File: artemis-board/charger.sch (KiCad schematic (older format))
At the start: 25 parts, among them J10 External NTC, J2 Thermistor, Q2 2N7002, SW2 SKRKAEE020, U3 LC709203FQH-01TWG, U4 TP4056, U8 XC6206P332MR

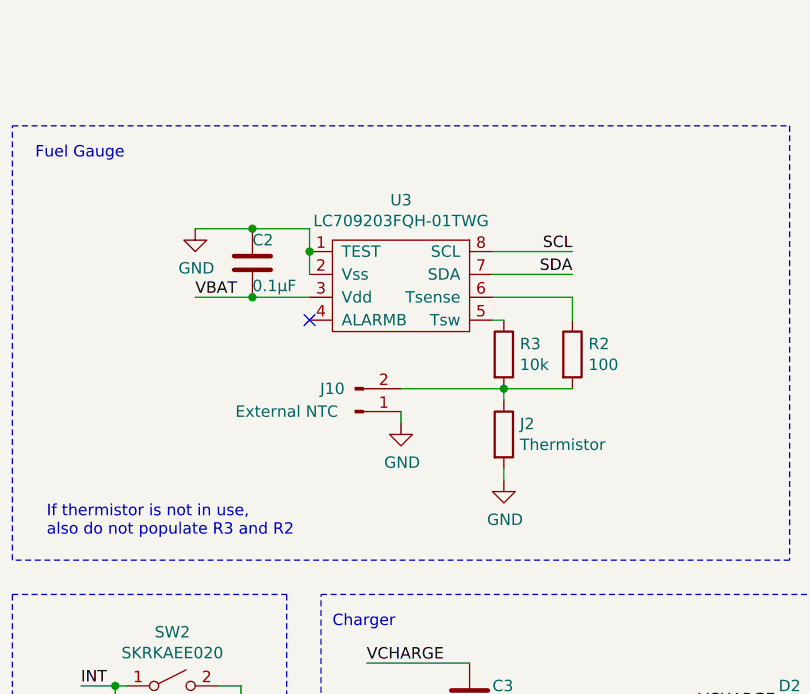
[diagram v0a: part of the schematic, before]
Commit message: removed lc709203 and added MAX17048
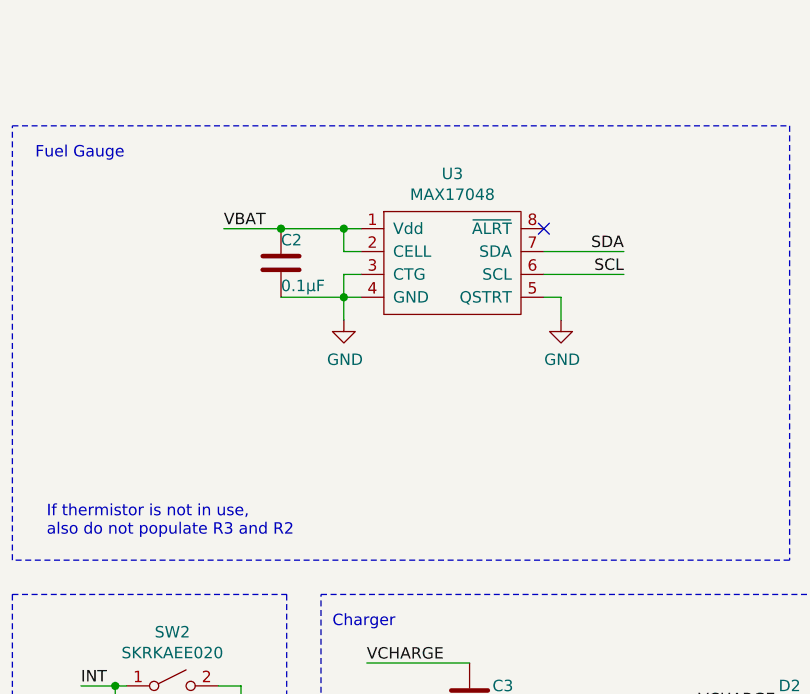
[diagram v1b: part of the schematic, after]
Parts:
- removed J10: External NTC, Connector_PinHeader_2.54mm:PinHeader_1x02_P2.54mm_Vertical, symbol Connector:Conn_01x02_Male
- removed J2: Thermistor, Resistor_SMD:R_0603_1608Metric_Pad1.05x0.95mm_HandSolder, symbol Device:R
- removed R2: 100, Resistor_SMD:R_0603_1608Metric_Pad1.05x0.95mm_HandSolder, symbol Device:R
- removed R3: 10k, Resistor_SMD:R_0603_1608Metric_Pad1.05x0.95mm_HandSolder, symbol Device:R
- removed U3: LC709203FQH-01TWG, Package_DFN_QFN:WDFN-8-1EP_4x3mm_P0.65mm_EP2.4x1.8mm, symbol LC709203FQH:LC709203FQH
- added U3: MAX17048, Package_DFN_QFN:TDFN-8-1EP_2x2mm_P0.5mm_EP0.8x1.2mm, symbol MAX17048:MAX17048
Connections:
- net GND: now also C2.2, U3.3 (CTG), U3.4 (GND), U3.5 (QSTRT); no longer C2.1
- net SCL: now also U3.6 (SCL)
- net SDA: now also U3.7 (SDA)
- net VBAT: now also C2.1, U3.1 (Vdd), U3.2 (CELL); no longer C2.2
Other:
- moved on the sheet: C2
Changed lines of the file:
@@
 	6350 5300 6350 5050
 Wire Wire Line
-	3300 2800 3550 2800
-Text Label 3300 2800 0    50   ~ 0
+	3425 2500 3675 2500
+Text Label 3425 2500 0    50   ~ 0
 VBAT
-Text Label 4950 2600 2    50   ~ 0
+Text Label 5175 2700 2    50   ~ 0
 SCL
-Text Label 4950 2700 2    50   ~ 0
+Text Label 5175 2600 2    50   ~ 0
 SDA
 Wire Wire Line
-	4950 2600 4600 2600
-Wire Wire Line
-	4950 2700 4600 2700
+	5175 2700 4825 2700
+Wire Wire Line
+	5175 2600 4825 2600
 Wire Notes Line
 	2500 2050 5900 2050
-NoConn ~ 3800 2900
-Connection ~ 3550 2800
-$Comp
-L LC709203FQH:LC709203FQH U3
-U 1 1 5F7E175C
-P 4200 2750
-F 0 "U3" H 4200 3125 50  0000 C CNN
-F 1 "LC709203FQH-01TWG" H 4200 3034 50  0000 C CNN
-F 2 "Package_DFN_QFN:WDFN-8-1EP_4x3mm_P0.65mm_EP2.4x1.8mm" H 4250 2500 50  0001 C CNN
-F 3 "https://www.onsemi.com/pub/Collateral/LC709203F-D.PDF" H 4200 2800 50  0001 C CNN
-F 4 "C152311" H 4200 2750 50  0001 C CNN "LCSC"
-	1    4200 2750
-	1    0    0    -1
-$EndComp
-$Comp
-L Device:R R2
-U 1 1 5F7E20B2
-P 4950 3050
-F 0 "R2" H 5020 3096 50  0000 L CNN
-F 1 "100" H 5020 3005 50  0000 L CNN
-F 2 "Resistor_SMD:R_0603_1608Metric_Pad1.05x0.95mm_HandSolder" V 4880 3050 50  0001 C CNN
-F 3 "~" H 4950 3050 50  0001 C CNN
-F 4 "C22775" H 4950 3050 50  0001 C CNN "LCSC"
-	1    4950 3050
-	1    0    0    -1
-$EndComp
-$Comp
-L Device:R R3
-U 1 1 5F7E249E
-P 4650 3050
-F 0 "R3" H 4720 3096 50  0000 L CNN
-F 1 "10k" H 4720 3005 50  0000 L CNN
-F 2 "Resistor_SMD:R_0603_1608Metric_Pad1.05x0.95mm_HandSolder" V 4580 3050 50  0001 C CNN
-F 3 "~" H 4650 3050 50  0001 C CNN
-F 4 "C25804" H 4650 3050 50  0001 C CNN "LCSC"
-	1    4650 3050
-	1    0    0    -1
-$EndComp
 $Comp
 L Device:C C2
 U 1 1 5F7E2A6A
-P 3550 2650
-F 0 "C2" H 3550 2750 50  0000 L CNN
-F 1 "0.1µF" H 3550 2550 50  0000 L CNN
-F 2 "Capacitor_SMD:C_0603_1608Metric_Pad1.05x0.95mm_HandSolder" H 3588 2500 50  0001 C CNN
-F 3 "~" H 3550 2650 50  0001 C CNN
-F 4 "C14858" H 3550 2650 50  0001 C CNN "LCSC"
-	1    3550 2650
-	1    0    0    -1
-$EndComp
-Wire Wire Line
-	4600 2900 4650 2900
-Wire Wire Line
-	4600 2800 4950 2800
-Wire Wire Line
-	4950 2800 4950 2900
-Wire Wire Line
-	4650 3200 4950 3200
-Wire Wire Line
-	3800 2800 3550 2800
-Wire Wire Line
-	3800 2700 3800 2600
-Wire Wire Line
-	3550 2500 3800 2500
-Wire Wire Line
-	3800 2500 3800 2600
-Connection ~ 3800 2600
+P 3675 2650
+F 0 "C2" H 3675 2750 50  0000 L CNN
+F 1 "0.1µF" H 3675 2550 50  0000 L CNN
+F 2 "Capacitor_SMD:C_0603_1608Metric_Pad1.05x0.95mm_HandSolder" H 3713 2500 50  0001 C CNN
+F 3 "~" H 3675 2650 50  0001 C CNN
+F 4 "C14858" H 3675 2650 50  0001 C CNN "LCSC"
+	1    3675 2650
+	1    0    0    -1
+$EndComp
 $Comp
 L power:GND #PWR0105
 U 1 1 5F7E81F4
-P 3300 2500
-F 0 "#PWR0105" H 3300 2250 50  0001 C CNN
-F 1 "GND" H 3305 2327 50  0000 C CNN
-F 2 "" H 3300 2500 50  0001 C CNN
-F 3 "" H 3300 2500 50  0001 C CNN
-	1    3300 2500
-	1    0    0    -1
-$EndComp
-Wire Wire Line
-	3300 2500 3550 2500
-Connection ~ 3550 2500
-$Comp
-L power:GND #PWR0104
-U 1 1 5F7EE01C
-P 4650 3600
-F 0 "#PWR0104" H 4650 3350 50  0001 C CNN
-F 1 "GND" H 4655 3427 50  0000 C CNN
-F 2 "" H 4650 3600 50  0001 C CNN
-F 3 "" H 4650 3600 50  0001 C CNN
-	1    4650 3600
+P 4900 2900
+F 0 "#PWR0105" H 4900 2650 50  0001 C CNN
+F 1 "GND" H 4905 2727 50  0000 C CNN
+F 2 "" H 4900 2900 50  0001 C CNN
+F 3 "" H 4900 2900 50  0001 C CNN
+	1    4900 2900
 	1    0    0    -1
 $EndComp
@@
 	0    1    1    0
 $EndComp
-$Comp
-L Device:R J2
-U 1 1 600A8086
-P 4650 3400
-F 0 "J2" H 4720 3446 50  0000 L CNN
-F 1 "Thermistor" H 4720 3355 50  0000 L CNN
-F 2 "Resistor_SMD:R_0603_1608Metric_Pad1.05x0.95mm_HandSolder" V 4580 3400 50  0001 C CNN
-F 3 "https://datasheet.lcsc.com/szlcsc/TDK-NTCG163JF103FT1_C76589.pdf" H 4650 3400 50  0001 C CNN
-F 4 "C76589" H 4650 3400 50  0001 C CNN "LCSC"
-	1    4650 3400
-	1    0    0    -1
-$EndComp
-Wire Wire Line
-	4650 3550 4650 3600
-Wire Wire Line
-	4650 3250 4650 3200
-Connection ~ 4650 3200
 Text Notes 6100 3900 0    50   ~ 0
 This cirquit automatically pulls down the INT line when first powerd on
@@
 If thermistor is not in use,\nalso do not populate R3 and R2
 $Comp
-L Connector:Conn_01x02_Male J?
-U 1 1 60103514
-P 4000 3300
-AR Path="/5F639CFE/60103514" Ref="J?"  Part="1"
-AR Path="/5F639F48/60103514" Ref="J10"  Part="1"
-F 0 "J10" H 3900 3200 50  0000 C CNN
-F 1 "External NTC" H 3700 3300 50  0000 C CNN
-F 2 "Connector_PinHeader_2.54mm:PinHeader_1x02_P2.54mm_Vertical" H 4000 3300 50  0001 C CNN
-F 3 "" H 4000 3300 50  0001 C CNN
-F 4 "" H 4000 3300 50  0001 C CNN "LCSC"
-F 5 "DNP" H 4000 3300 50  0001 C CNN "DNP"
-	1    4000 3300
-	1    0    0    1
-$EndComp
-Wire Wire Line
-	4650 3200 4200 3200
-$Comp
 L power:GND #PWR0131
 U 1 1 60107260
-P 4200 3350
-F 0 "#PWR0131" H 4200 3100 50  0001 C CNN
-F 1 "GND" H 4205 3177 50  0000 C CNN
-F 2 "" H 4200 3350 50  0001 C CNN
-F 3 "" H 4200 3350 50  0001 C CNN
-	1    4200 3350
-	1    0    0    -1
-$EndComp
-Wire Wire Line
-	4200 3300 4200 3350
+P 3950 2900
+F 0 "#PWR0131" H 3950 2650 50  0001 C CNN
+F 1 "GND" H 3955 2727 50  0000 C CNN
+F 2 "" H 3950 2900 50  0001 C CNN
+F 3 "" H 3950 2900 50  0001 C CNN
+	1    3950 2900
+	1    0    0    -1
+$EndComp
 $Comp
 L Switch:SW_SPST SW?
@@
 Wire Notes Line
 	2000 6050 4350 6050
+$Comp
+L MAX17048:MAX17048 U?
+U 1 1 626AEF97
+P 4425 2325
+AR Path="/626AEF97" Ref="U?"  Part="1"
+AR Path="/5F639F48/626AEF97" Ref="U3"  Part="1"
+F 0 "U3" H 4425 2390 50  0000 C CNN
+F 1 "MAX17048" H 4425 2299 50  0000 C CNN
+F 2 "Package_DFN_QFN:TDFN-8-1EP_2x2mm_P0.5mm_EP0.8x1.2mm" H 4425 2325 50  0001 C CNN
+F 3 "https://datasheets.maximintegrated.com/en/ds/MAX17048-MAX17049.pdf" H 4425 2325 50  0001 C CNN
+	1    4425 2325
+	1    0    0    -1
+$EndComp
+NoConn ~ 4825 2500
+Wire Wire Line
+	4900 2900 4900 2800
+Wire Wire Line
+	4900 2800 4825 2800
+Wire Wire Line
+	3950 2900 3950 2800
+Wire Wire Line
+	3950 2800 4025 2800
+Wire Wire Line
+	3950 2800 3950 2700
+Wire Wire Line
+	3950 2700 4025 2700
+Connection ~ 3950 2800
+Wire Wire Line
+	3675 2800 3950 2800
+Wire Wire Line
+	3675 2500 3950 2500
+Wire Wire Line
+	4025 2600 3950 2600
+Wire Wire Line
+	3950 2600 3950 2500
+Connection ~ 3950 2500
+Wire Wire Line
+	3950 2500 4025 2500
+Connection ~ 3675 2500
 $EndSCHEMATC

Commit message: + temperature sensor, i2c header - esp voltage  measurement...
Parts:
- added C26: 0.1µF, Capacitor_SMD:C_0603_1608Metric_Pad1.05x0.95mm_HandSolder, symbol Device:C
- added J2: I2c, Connector_PinSocket_2.54mm:PinSocket_1x04_P2.54mm_Vertical, symbol Connector:Conn_01x04_Female
- added U13: TMP75, Package_SO:SOIC-8_3.9x4.9mm_P1.27mm, symbol Sensor_Temperature:LM75B
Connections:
- net 3v3_I2C: now also C26.1, J2.1 (Pin_1), U13.8 (+Vs)
- net GND: now also C26.2, J2.2 (Pin_2), U13.4 (GND), U13.5 (A2), U13.6 (A1), U13.7 (A0)
- net SCL: now also J2.3 (Pin_3), U13.2 (SCL)
- net SDA: now also J2.4 (Pin_4), U13.1 (SDA)
- no-connect marks 1 -> 2
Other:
- note added: "I2c connector"
- note added: "Temperature sensor"
- note removed: "If thermistor is not in use,\nalso do not populate R3 and R2"
- moved on the sheet: C2, C4, D3, Q2, R7, U3
